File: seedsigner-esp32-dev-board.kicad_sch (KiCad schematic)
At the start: 11 parts, among them J1 Conn_01x06, J2 Conn_01x08, U1 ESP32-S2-SAOLA-1M, U2 OV_CAMERA, U3 RASPBERRY_PI_3_MODEL_B+

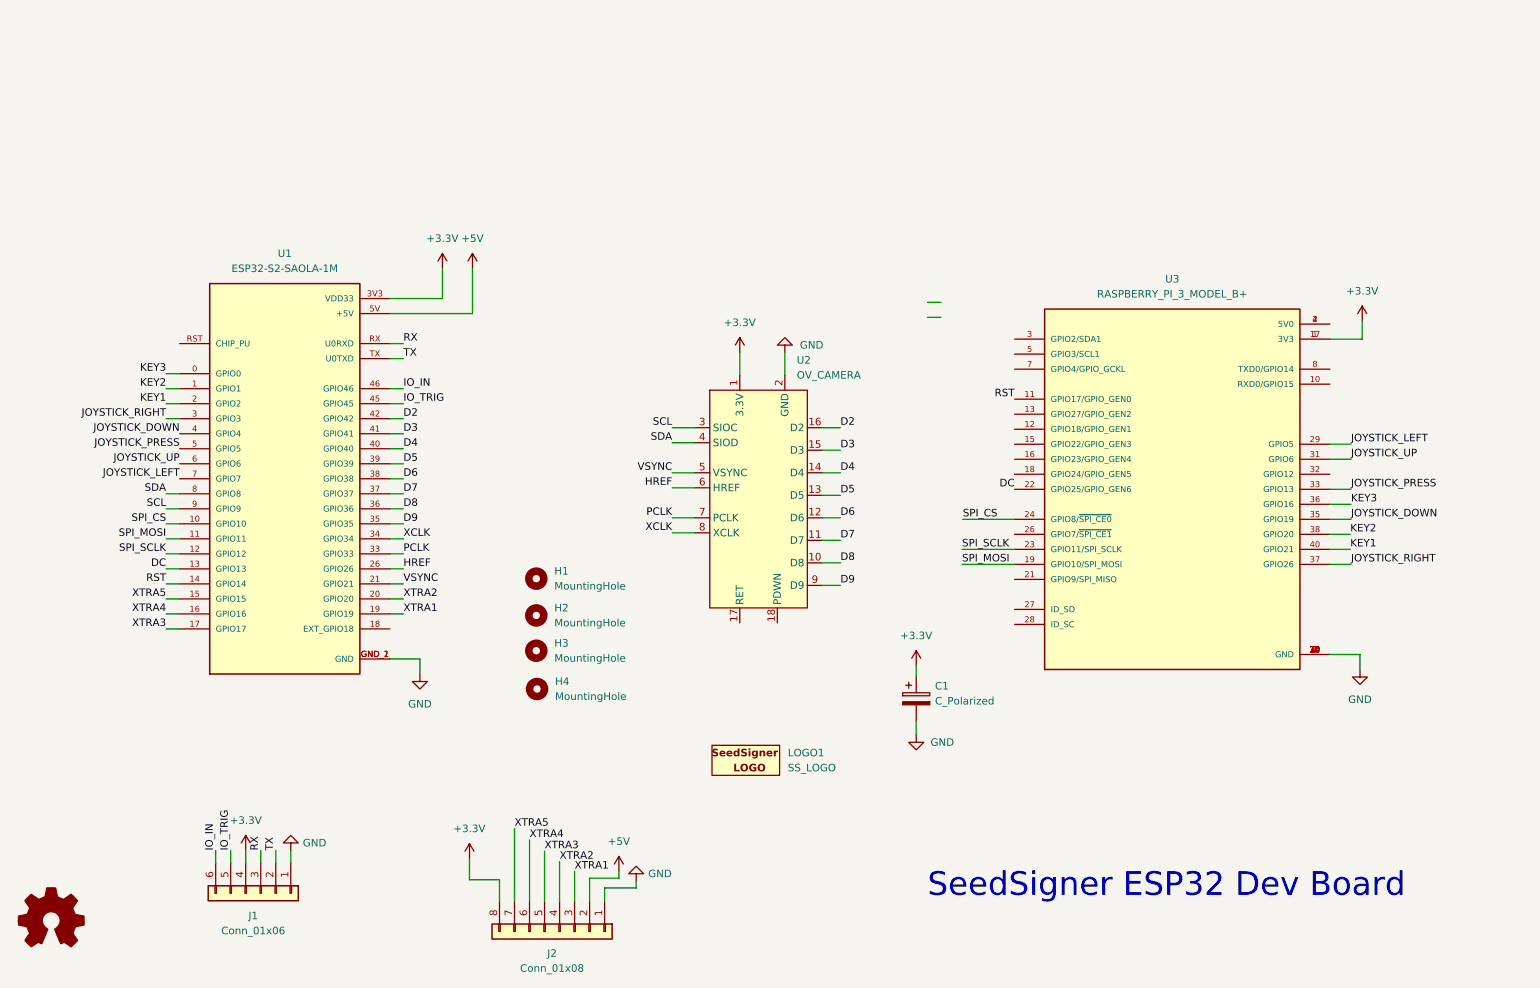
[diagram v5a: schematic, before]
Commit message: add gerbers and fix RESET and PWM pin
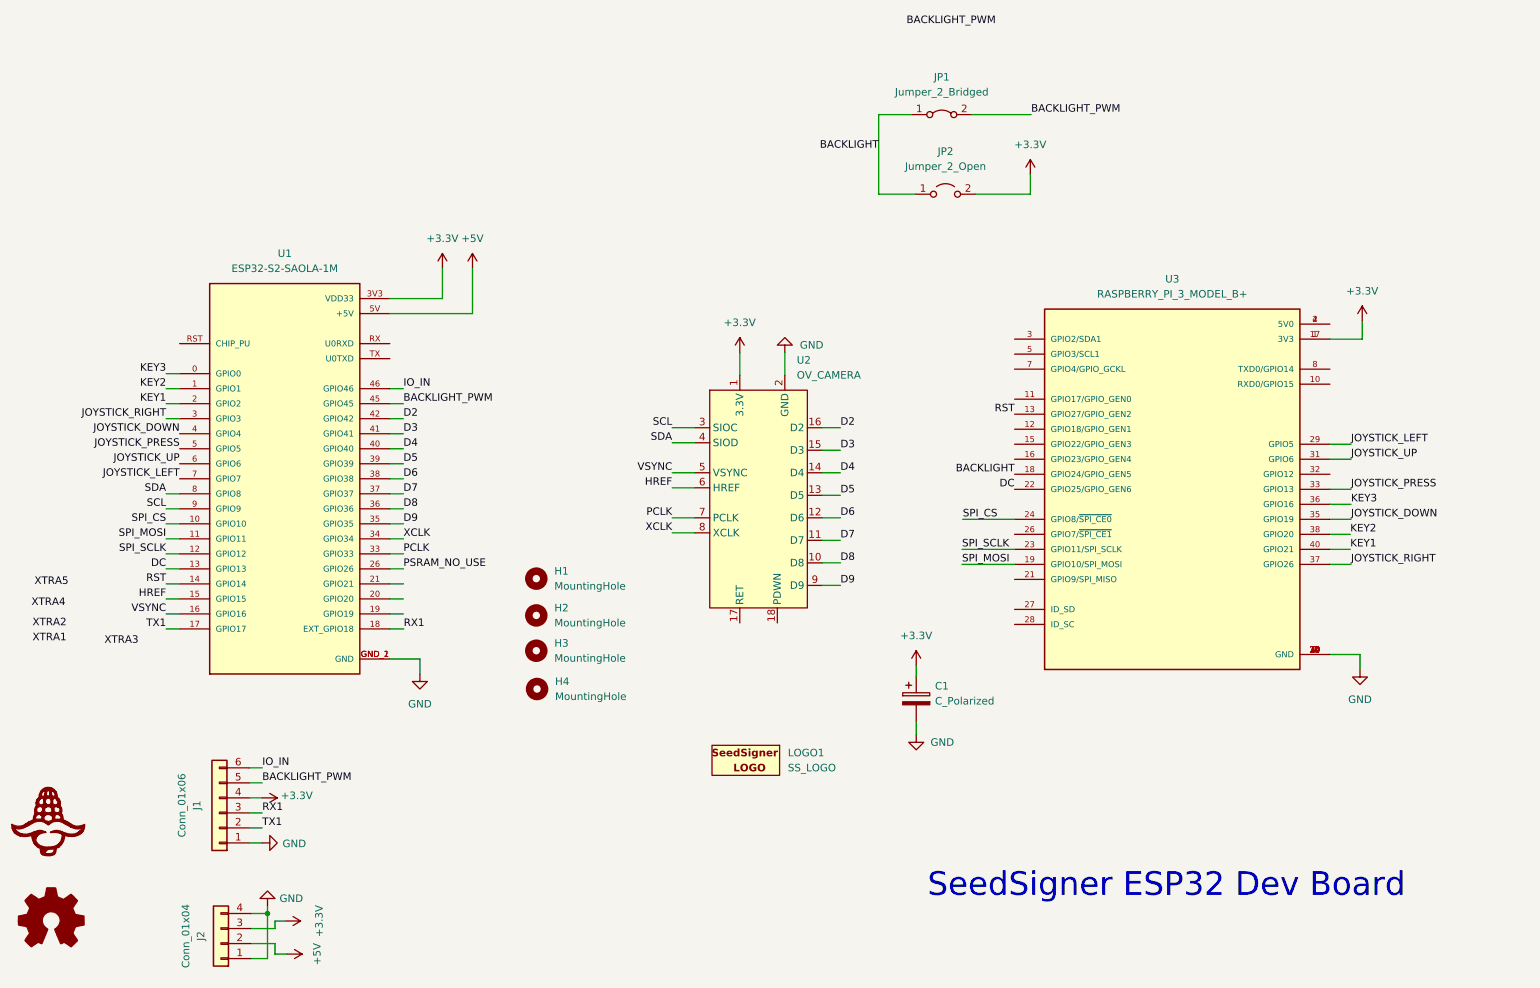
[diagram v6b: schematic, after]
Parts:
- removed J2: Conn_01x08, Connector_PinSocket_2.00mm:PinSocket_1x08_P2.00mm_Vertical, symbol Connector_Generic:Conn_01x08
- added J2: Conn_01x04, Connector_PinHeader_2.54mm:PinHeader_1x04_P2.54mm_Vertical, symbol Connector_Generic:Conn_01x04
- added JP1: Jumper_2_Bridged, Jumper:SolderJumper-2_P1.3mm_Bridged_Pad1.0x1.5mm, symbol Jumper:Jumper_2_Bridged
- added JP2: Jumper_2_Open, Jumper:SolderJumper-2_P1.3mm_Open_Pad1.0x1.5mm, symbol Jumper:Jumper_2_Open
- added LOGO2: CORN-LOGO, SeedSigner:corn-logo, symbol SeedSigner:CORN-LOGO
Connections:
- net +3.3V: now also J2.3 (Pin_3), JP2.2 (B)
- net +5V: now also J2.2 (Pin_2)
- net GND: now also J2.1 (Pin_1), J2.4 (Pin_4)
- net HREF: now also U1.15 (GPIO15); no longer U1.26 (GPIO26)
- net RST: now also U3.13 (GPIO27/GPIO_GEN2); no longer U3.11 (GPIO17/GPIO_GEN0)
- net VSYNC: now also U1.16 (GPIO16); no longer U1.21 (GPIO21)
- net XTRA1: no longer U1.19 (GPIO19)
- net XTRA2: no longer U1.20 (GPIO20)
- net XTRA3: no longer U1.17 (GPIO17)
- net XTRA4: no longer U1.16 (GPIO16)
- net XTRA5: no longer U1.15 (GPIO15)
- net BACKLIGHT: now reaches U3.18 (GPIO24/GPIO_GEN5)
- net BACKLIGHT: now also JP1.1 (A), JP2.1 (A)
- net RX1: now reaches U1.18 (EXT_GPIO18)
- net RX1: now also J1.3 (Pin_3)
- net IO_TRIG renamed BACKLIGHT_PWM
- net BACKLIGHT_PWM: now also JP1.2 (B)
- net RX: no longer names the net of U1.RX (U0RXD)
- net RX: no longer J1.3 (Pin_3)
- net TX: no longer names the net of U1.TX (U0TXD)
- net TX: no longer J1.2 (Pin_2)
- new net PSRAM_NO_USE: U1.26 (GPIO26)
- new net TX1: J1.2 (Pin_2), U1.17 (GPIO17)
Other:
- moved on the sheet: J1
